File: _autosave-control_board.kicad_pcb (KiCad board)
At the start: 2 copper layers, 124.6 x 131.9 mm, 88 parts, among them J1 Conn_01x02_Female, J10 Conn_02x04_Odd_Even, J11 Screw_Terminal_01x02, J12 Conn_01x03, J13 Conn_01x03, J14 Conn_01x03, J15 Conn_02x04_Odd_Even, J16 Conn_02x04_Odd_Even, J17 Conn_01x03, J18 Conn_01x03, J19 Conn_02x03_Odd_Even, J2 Conn_02x25_Odd_Even, J3 Conn_02x25_Odd_Even, J4 Conn_01x01, J5 Conn_01x01, J6 Conn_01x01, J7 Conn_01x01, J8 Conn_01x03, J9 Conn_01x03, Q1 2N2219, Q10 2N2219, Q11 2N2219, Q12 2N2219, Q2 2N2219, Q3 2N2219, Q4 2N2219, Q5 2N2219, Q6 2N2219, Q7 2N2219, Q8 2N2219, Q9 2N2219, SW1 SW_Push, SW2 SW_Push, SW3 SW_Push, SW4 SW_Push, U1 LM1117-3.3

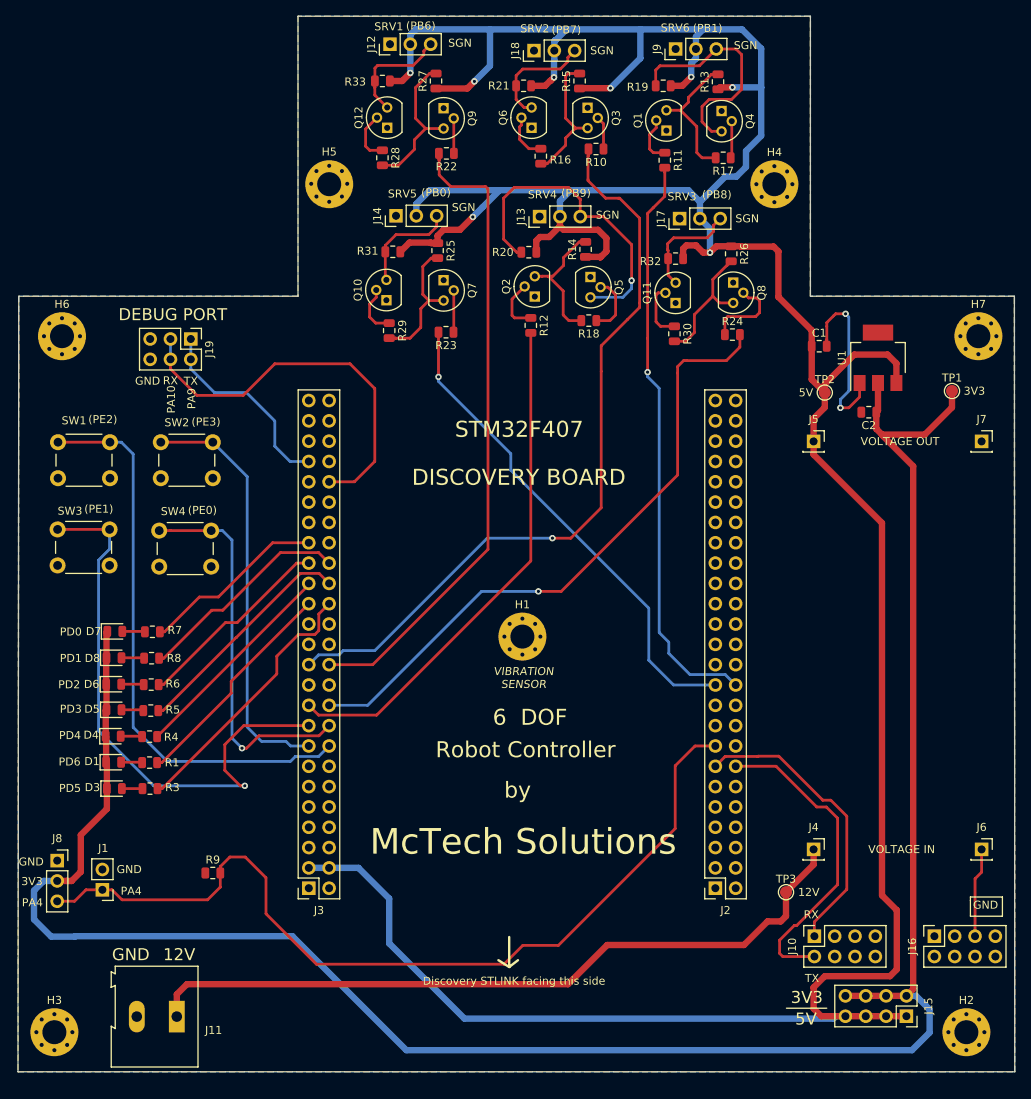
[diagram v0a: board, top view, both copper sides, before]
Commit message: added ESP8266 circuit
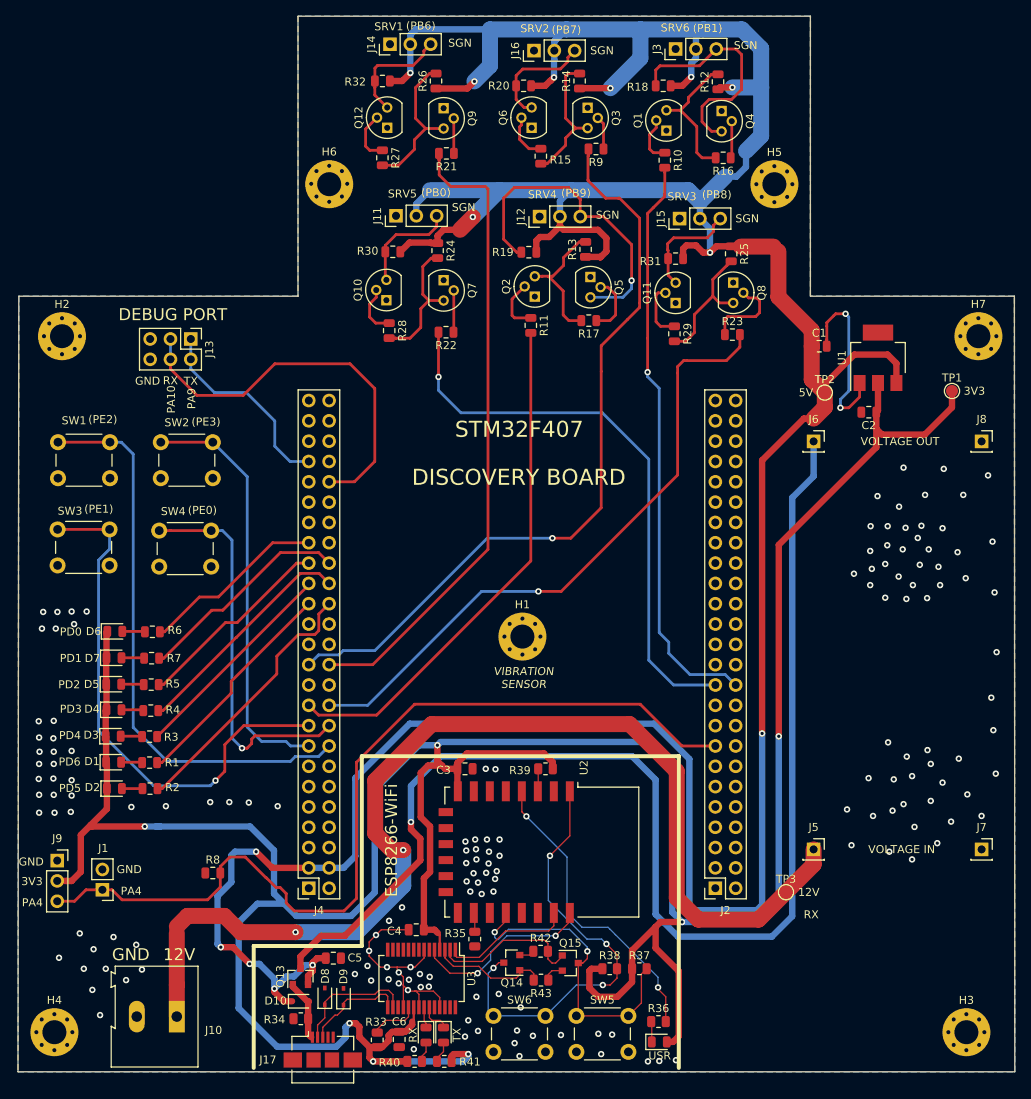
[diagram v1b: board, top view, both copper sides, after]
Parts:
- removed the J10 at (128.0, 140.0)
- removed the J15 at (139.5, 150.0)
- removed the J16 at (143.0, 140.0)
- removed REF**: OSHW-Logo2_24.3x20mm_SilkScreen, Symbol:OSHW-Logo2_24.3x20mm_SilkScreen
- added C3: 100nF, Capacitor_SMD:C_0805_2012Metric, F.Cu at (84.3, 119.1)
- added C4: 100nF, Capacitor_SMD:C_0805_2012Metric, F.Cu at (78.2, 139.2)
- added C5: 10uF, Capacitor_SMD:C_0805_2012Metric, F.Cu at (67.9, 142.7)
- added C6: 100nF, Capacitor_SMD:C_0805_2012Metric, F.Cu at (76.1, 152.9)
- added D10: 1N4148WS, Diode_SMD:D_SOD-323, F.Cu at (63.8, 148.1)
- added D8: 1N4448WS, Diode_SMD:D_SOD-323, F.Cu at (66.8, 147.5)
- added D9: 1N4448WS, Diode_SMD:D_SOD-323, F.Cu at (69.1, 147.6)
- added J17: USB_B_Micro, Connector_USB:USB_Micro-B_Amphenol_10104110_Horizontal, F.Cu at (66.5, 154.2)
- added Q13: BSS84, Package_TO_SOT_SMD:SOT-23, F.Cu at (63.8, 145.0)
- added Q14: S8050, Package_TO_SOT_SMD:SOT-23, F.Cu at (90.2, 143.3)
- added Q15: S8050, Package_TO_SOT_SMD:SOT-23, F.Cu at (97.5, 143.4)
- added R33: 10K, Resistor_SMD:R_0805_2012Metric, F.Cu at (73.4, 153.0)
- added R34: 100K, Resistor_SMD:R_0805_2012Metric, F.Cu at (63.8, 150.3)
- added R35: 10K, Resistor_SMD:R_0805_2012Metric, F.Cu at (85.5, 140.4)
- added R36: 200, Resistor_SMD:R_0805_2012Metric, F.Cu at (108.5, 150.7)
- added R37: 10K, Resistor_SMD:R_0805_2012Metric, F.Cu at (106.1, 144.1)
- added R38: 10K, Resistor_SMD:R_0805_2012Metric, F.Cu at (102.4, 144.1)
- added R39: 10K, Resistor_SMD:R_0805_2012Metric, F.Cu at (94.4, 119.1)
- added R40: 200, Resistor_SMD:R_0805_2012Metric, F.Cu at (78.0, 155.7)
- added R41: 200, Resistor_SMD:R_0805_2012Metric, F.Cu at (81.7, 155.7)
- added R42: 10K, Resistor_SMD:R_0805_2012Metric, F.Cu at (93.8, 141.9)
- added R43: 10K, Resistor_SMD:R_0805_2012Metric, F.Cu at (93.8, 145.5)
- added RX: LED, LED_SMD:LED_0805_2012Metric, F.Cu at (79.5, 152.3)
- added SW5: SW_Push, Button_Switch_THT:SW_PUSH_6mm, F.Cu at (98.2, 150.0)
- added SW6: SW_Push, Button_Switch_THT:SW_PUSH_6mm, F.Cu at (87.9, 150.0)
- added TX: LED, LED_SMD:LED_0805_2012Metric, F.Cu at (81.6, 152.3)
- added U2: ESP-12E, RF_Module:ESP-12E, F.Cu at (93.9, 129.5)
- added U3: FT232RL, Package_SO:SSOP-28_5.3x10.2mm_P0.65mm, F.Cu at (78.9, 145.3)
- added USR: LED, LED_SMD:LED_0805_2012Metric, F.Cu at (108.6, 153.2)
- renumbered D3 to D2, D4 to D3, D5 to D4, D6 to D5, D7 to D6, D8 to D7, H6 to H2, H2 to H3, H3 to H4, H4 to H5, H5 to H6, J11 to J10, J14 to J11, J13 to J12, J19 to J13, J12 to J14, J17 to J15, J18 to J16, J9 to J3, J3 to J4, J4 to J5, J5 to J6, J6 to J7, J7 to J8, J8 to J9, R11 to R10, R12 to R11, R13 to R12, R14 to R13, R15 to R14, R16 to R15, R17 to R16, R18 to R17, R19 to R18, R20 to R19, R3 to R2, R21 to R20, R22 to R21, R23 to R22, R24 to R23, R25 to R24, R26 to R25, R27 to R26, R28 to R27, R29 to R28, R30 to R29, R4 to R3, R31 to R30, R32 to R31, R33 to R32, R5 to R4, R6 to R5, R7 to R6, R8 to R7, R9 to R8, R10 to R9
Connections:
- J2 pad 10: Net-(J2-Pad10) -> (no net)
- J2 pad 11: Net-(J2-Pad11) -> (no net)
- J2 pad 12: Net-(J2-Pad12) -> (no net)
- J2 pad 13: USART_TX -> (no net)
- J2 pad 14: USART_RX -> (no net)
- J2 pad 16: Net-(J2-Pad16) -> (no net)
- J2 pad 17: Net-(J2-Pad17) -> (no net)
- J2 pad 18: Net-(J2-Pad18) -> (no net)
- J2 pad 19: Net-(J2-Pad19) -> (no net)
- J2 pad 20: Net-(J2-Pad20) -> (no net)
- J2 pad 23: Net-(J2-Pad23) -> (no net)
- J2 pad 25: Net-(J2-Pad25) -> (no net)
- J2 pad 26: Net-(J2-Pad26) -> (no net)
- J2 pad 27: Net-(J2-Pad27) -> (no net)
- J2 pad 28: Net-(J2-Pad28) -> (no net)
- J2 pad 29: Net-(J2-Pad29) -> (no net)
- J2 pad 3: Net-(J2-Pad3) -> (no net)
- J2 pad 30: Net-(J2-Pad30) -> (no net)
- J2 pad 31: Net-(J2-Pad31) -> (no net)
- J2 pad 32: Net-(J2-Pad32) -> (no net)
- J2 pad 33: Net-(J2-Pad33) -> (no net)
- J2 pad 34: Net-(J2-Pad34) -> (no net)
- J2 pad 35: Net-(J2-Pad35) -> (no net)
- J2 pad 36: Net-(J2-Pad36) -> (no net)
- J2 pad 37: Net-(J2-Pad37) -> (no net)
- J2 pad 38: Net-(J2-Pad38) -> (no net)
- J2 pad 39: Net-(J2-Pad39) -> (no net)
- J2 pad 4: Net-(J2-Pad4) -> (no net)
- J2 pad 40: Net-(J2-Pad40) -> (no net)
- J2 pad 41: Net-(J2-Pad41) -> (no net)
- J2 pad 42: Net-(J2-Pad42) -> (no net)
- J2 pad 43: Net-(J2-Pad43) -> (no net)
- J2 pad 44: Net-(J2-Pad44) -> (no net)
- J2 pad 45: Net-(J2-Pad45) -> (no net)
- J2 pad 46: Net-(J2-Pad46) -> (no net)
- J2 pad 47: Net-(J2-Pad47) -> (no net)
- J2 pad 48: Net-(J2-Pad48) -> (no net)
- J2 pad 5: Net-(J2-Pad5) -> (no net)
- J2 pad 7: Net-(J2-Pad7) -> (no net)
- J2 pad 8: Net-(J2-Pad8) -> (no net)
- J2 pad 9: Net-(J2-Pad9) -> (no net)
- J4 pad 10: Net-(J3-Pad10) -> (no net)
- J4 pad 11: Net-(J3-Pad11) -> (no net)
- J4 pad 12: Net-(J3-Pad12) -> (no net)
- J4 pad 13: Net-(J3-Pad13) -> (no net)
- J4 pad 14: Net-(J3-Pad14) -> (no net)
- J4 pad 21: Net-(J3-Pad21) -> (no net)
- J4 pad 22: Net-(J3-Pad22) -> (no net)
- J4 pad 25: Net-(J3-Pad25) -> (no net)
- J4 pad 26: Net-(J3-Pad26) -> (no net)
- J4 pad 27: Net-(J3-Pad27) -> (no net)
- J4 pad 28: Net-(J3-Pad28) -> (no net)
- J4 pad 36: Net-(J3-Pad36) -> (no net)
- J4 pad 37: Net-(J3-Pad37) -> (no net)
- J4 pad 38: Net-(J3-Pad38) -> (no net)
- J4 pad 39: Net-(J3-Pad39) -> (no net)
- J4 pad 40: Net-(J3-Pad40) -> (no net)
- J4 pad 41: Net-(J3-Pad41) -> (no net)
- J4 pad 44: Net-(J3-Pad44) -> (no net)
- J4 pad 45: Net-(J3-Pad45) -> (no net)
- J4 pad 46: Net-(J3-Pad46) -> (no net)
- J4 pad 47: Net-(J3-Pad47) -> (no net)
- J4 pad 48: Net-(J3-Pad48) -> (no net)
- J4 pad 5: Net-(J3-Pad5) -> (no net)
- J4 pad 6: Net-(J3-Pad6) -> (no net)
- J4 pad 7: Net-(J3-Pad7) -> (no net)
- J4 pad 8: Net-(J3-Pad8) -> (no net)
- J4 pad 9: Net-(J3-Pad9) -> (no net)
- J6 pad 1: +5V -> VIN
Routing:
- net VIN: track 0.00 -> 161.1 mm, vias 0 -> 1
- net +3V3: track 267.0 -> 409.0 mm, vias 0 -> 7
- net ESP_RST: track 0.00 -> 54.6 mm, vias 0 -> 4
- net +12V: track 92.8 -> 140.7 mm, vias 0 -> 2
- net USART_RX: track 40.0 -> 0.00 mm
- net GPIO0: track 0.00 -> 39.6 mm, vias 0 -> 2
- net GPIO16: track 0.00 -> 38.1 mm, vias 0 -> 2
- net USART_TX: track 36.7 -> 0.00 mm
- net +5V: track 438.9 -> 462.6 mm, vias 8 -> 14
- net ESP_TX: track 0.00 -> 23.1 mm, vias 0 -> 2
- net GND: track 34.0 -> 53.3 mm, vias 2 -> 161
- net DTR: track 0.00 -> 19.0 mm
- net ESP_RX: track 0.00 -> 16.4 mm
- net D-: track 0.00 -> 15.7 mm
- net RTS: track 0.00 -> 14.9 mm
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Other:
- net class Default: trace_width 0.35 -> 0.15
- net class Power: trace_width 0.8 -> 0.3
- rule trace_min: 0.2 -> 0.1
- board text added: "ESP8266-WiFi"
- board text removed: "6 DOF"
- board text removed: "Discovery STLINK facing this side"
- board text removed: "McTech Solutions"
- board text removed: "Robot Controller"
- board text removed: "by"
